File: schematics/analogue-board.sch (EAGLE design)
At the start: 81 parts, among them U1 L78S09

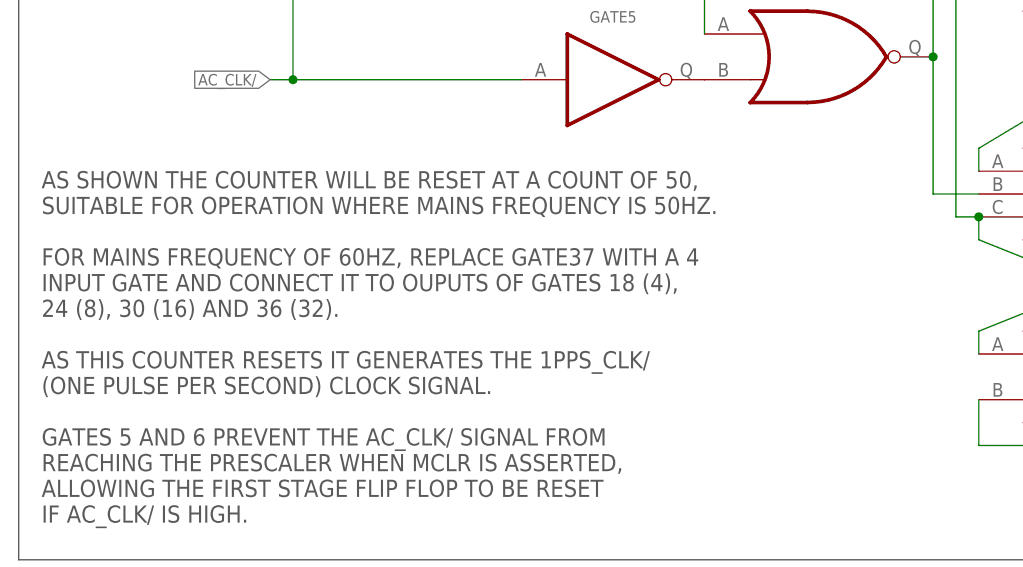
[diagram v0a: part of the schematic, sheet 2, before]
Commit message: Fixed notes for prescaler, references to incorrect gate numbers.
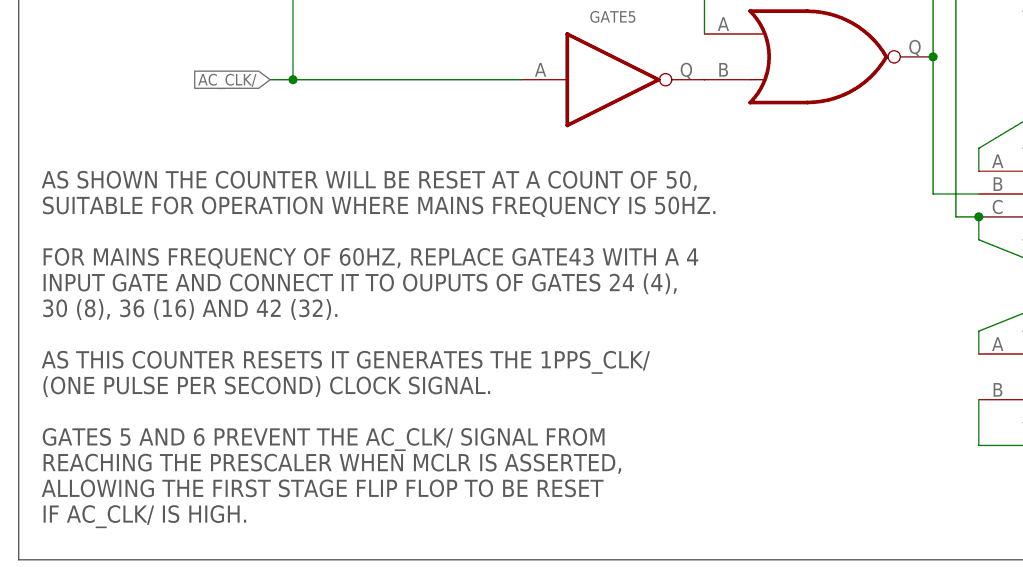
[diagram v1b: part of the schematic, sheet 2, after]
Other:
- note added: "AS SHOWN THE COUNTER WILL BE RESET AT A COUNT OF 50, SUITABLE FOR OPERATION WHERE MAINS FREQUENCY IS 50HZ. FOR MAINS FREQUENCY OF 60HZ, REPLACE GATE43 WITH A 4 INPUT GATE AND CONNECT IT TO OUPUTS OF GATES 24 (4), 30 (8), 36 (16) AND 42 (32). AS THIS COUNTER RESETS IT GENERATES THE 1PPS_CLK/ (ONE PULSE PER SECOND) CLOCK SIGNAL. GATES 5 AND 6 PREVENT THE AC_CLK/ SIGNAL FROM REACHING THE PRESCALER W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"
- note removed: "AS SHOWN THE COUNTER WILL BE RESET AT A COUNT OF 50, SUITABLE FOR OPERATION WHERE MAINS FREQUENCY IS 50HZ. FOR MAINS FREQUENCY OF 60HZ, REPLACE GATE37 WITH A 4 INPUT GATE AND CONNECT IT TO OUPUTS OF GATES 18 (4), 24 (8), 30 (16) AND 36 (32). AS THIS COUNTER RESETS IT GENERATES THE 1PPS_CLK/ (ONE PULSE PER SECOND) CLOCK SIGNAL. GATES 5 AND 6 PREVENT THE AC_CLK/ SIGNAL FROM REACHING THE PRESCALER W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"
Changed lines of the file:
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@@
 <text x="25.4" y="185.42" size="1.905" layer="97" align="top-left">AS SHOWN THE COUNTER WILL BE RESET AT A COUNT OF 50,
 SUITABLE FOR OPERATION WHERE MAINS FREQUENCY IS 50HZ.
-FOR MAINS FREQUENCY OF 60HZ, REPLACE GATE37 WITH A 4
-INPUT GATE AND CONNECT IT TO OUPUTS OF GATES 18 (4),
-24 (8), 30 (16) AND 36 (32).
+FOR MAINS FREQUENCY OF 60HZ, REPLACE GATE43 WITH A 4
+INPUT GATE AND CONNECT IT TO OUPUTS OF GATES 24 (4),
+30 (8), 36 (16) AND 42 (32).
 AS THIS COUNTER RESETS IT GENERATES THE 1PPS_CLK/
 (ONE PULSE PER SECOND) CLOCK SIGNAL.

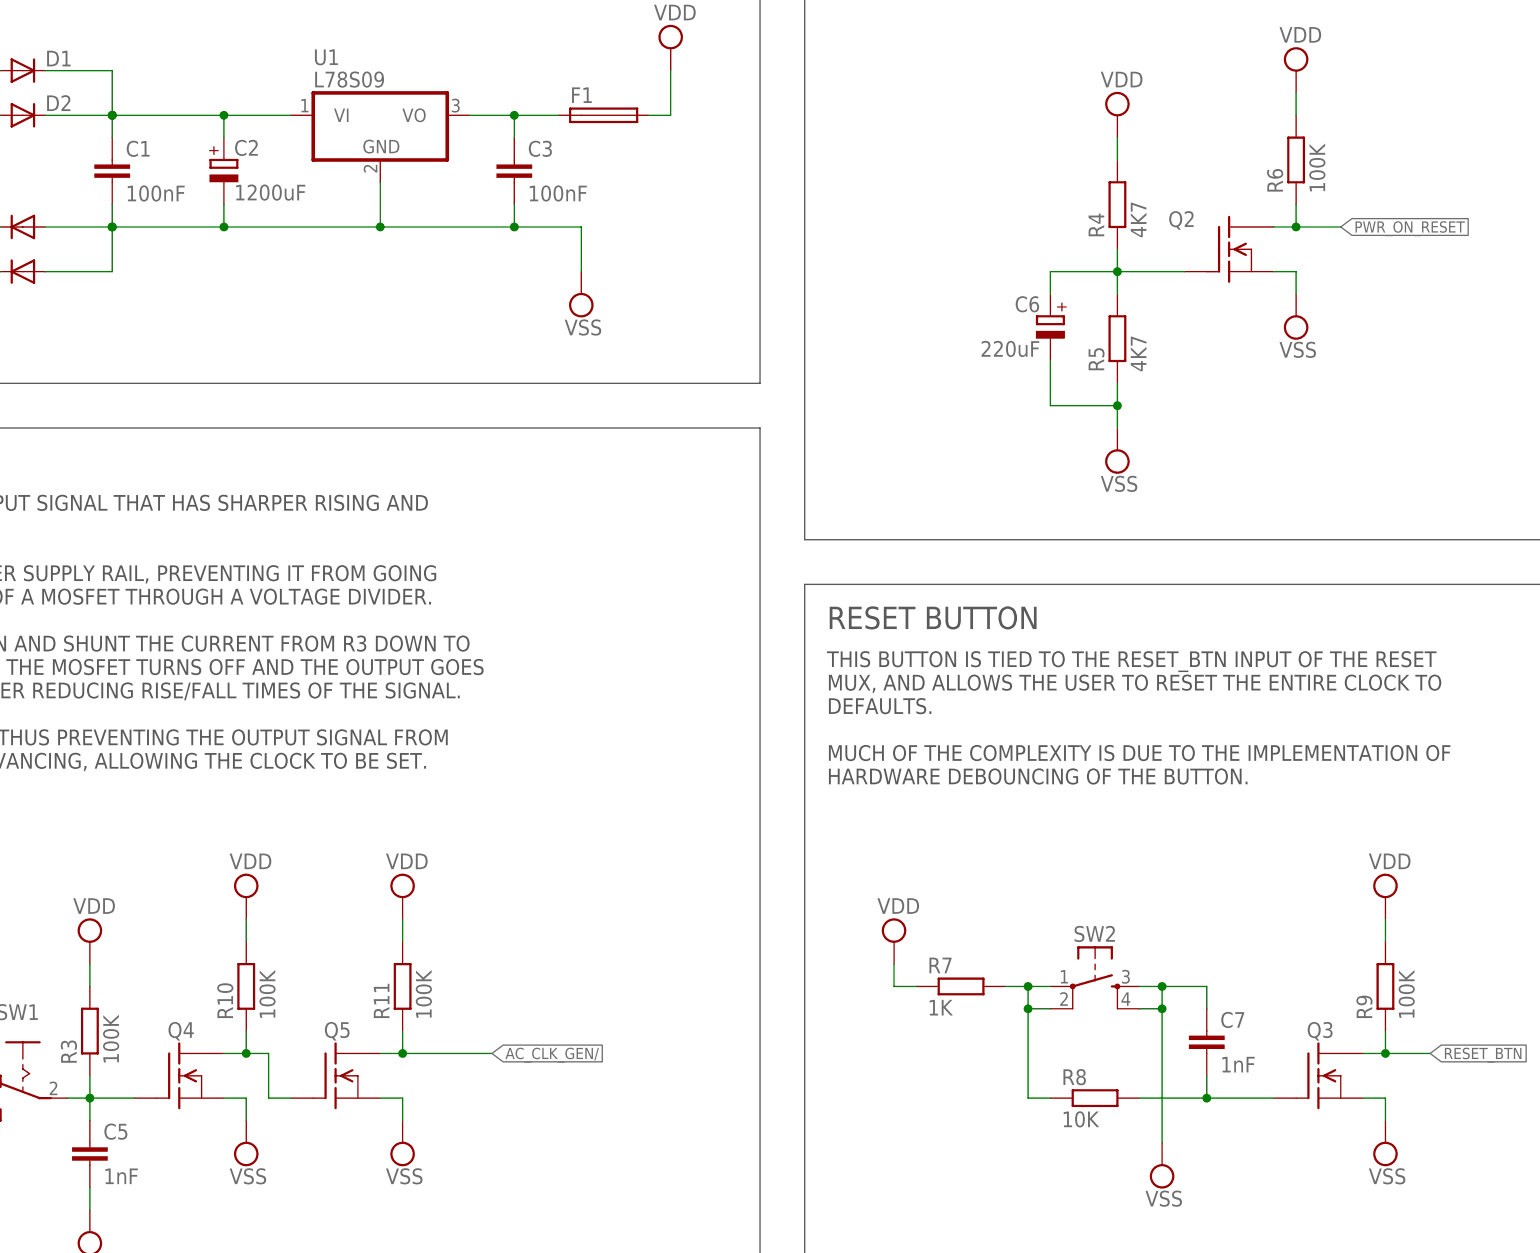
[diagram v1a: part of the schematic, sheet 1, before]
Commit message: Fix some component designators on the analogue board.
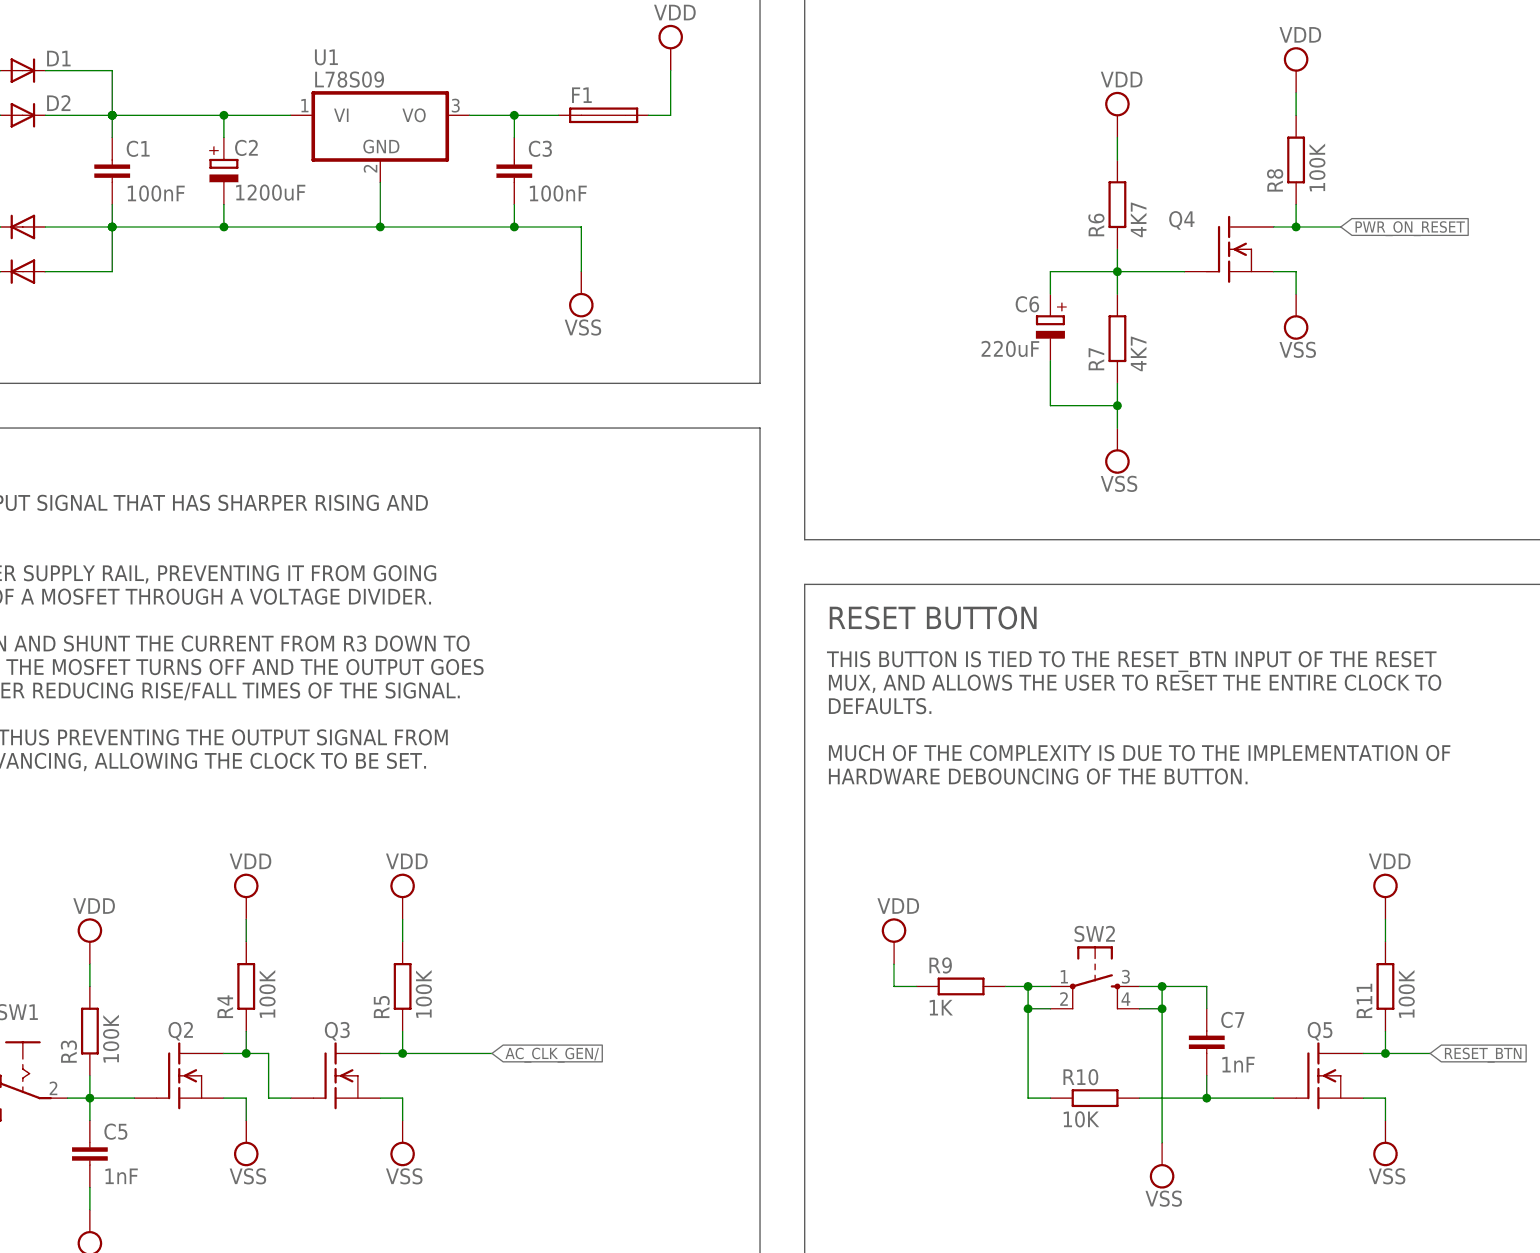
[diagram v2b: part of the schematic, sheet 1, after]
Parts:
- R10: value 100K -> 10K
- R4, R5: value 4K7 -> 100K
- R6: value 100K -> 4K7
- R7: value 1K -> 4K7
- R8: value 10K -> 100K
- R9: value 100K -> 1K
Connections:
- net AC_CLK_GEN/: now also Q3.D, R5.1; no longer Q5.D, R11.1
- net N$1: now also Q2.G; no longer Q4.G
- net N$12: now also R10.1, R9.2; no longer R7.2, R8.1
- net N$13: now also Q2.D, Q3.G, R4.1; no longer Q4.D, Q5.G, R10.1
- net N$15: now also Q5.G, R10.2; no longer Q3.G, R8.2
- net N$3: now also Q4.G, R6.1, R7.2; no longer Q2.G, R4.1, R5.2
- net PWR_ON_RESET: now also Q4.D, R8.1; no longer Q2.D, R6.1
- net RESET_BTN: now also Q5.D, R11.1; no longer Q3.D, R9.1
- net VDD: now also R5.2, R8.2, R9.1; no longer R10.2, R7.1, R9.2
- net VSS: now also R7.1; no longer R5.1
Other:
- moved on the sheet: Q2, Q3, Q4, Q5, R10, R11, R4, R5, R6, R7, R8, R9

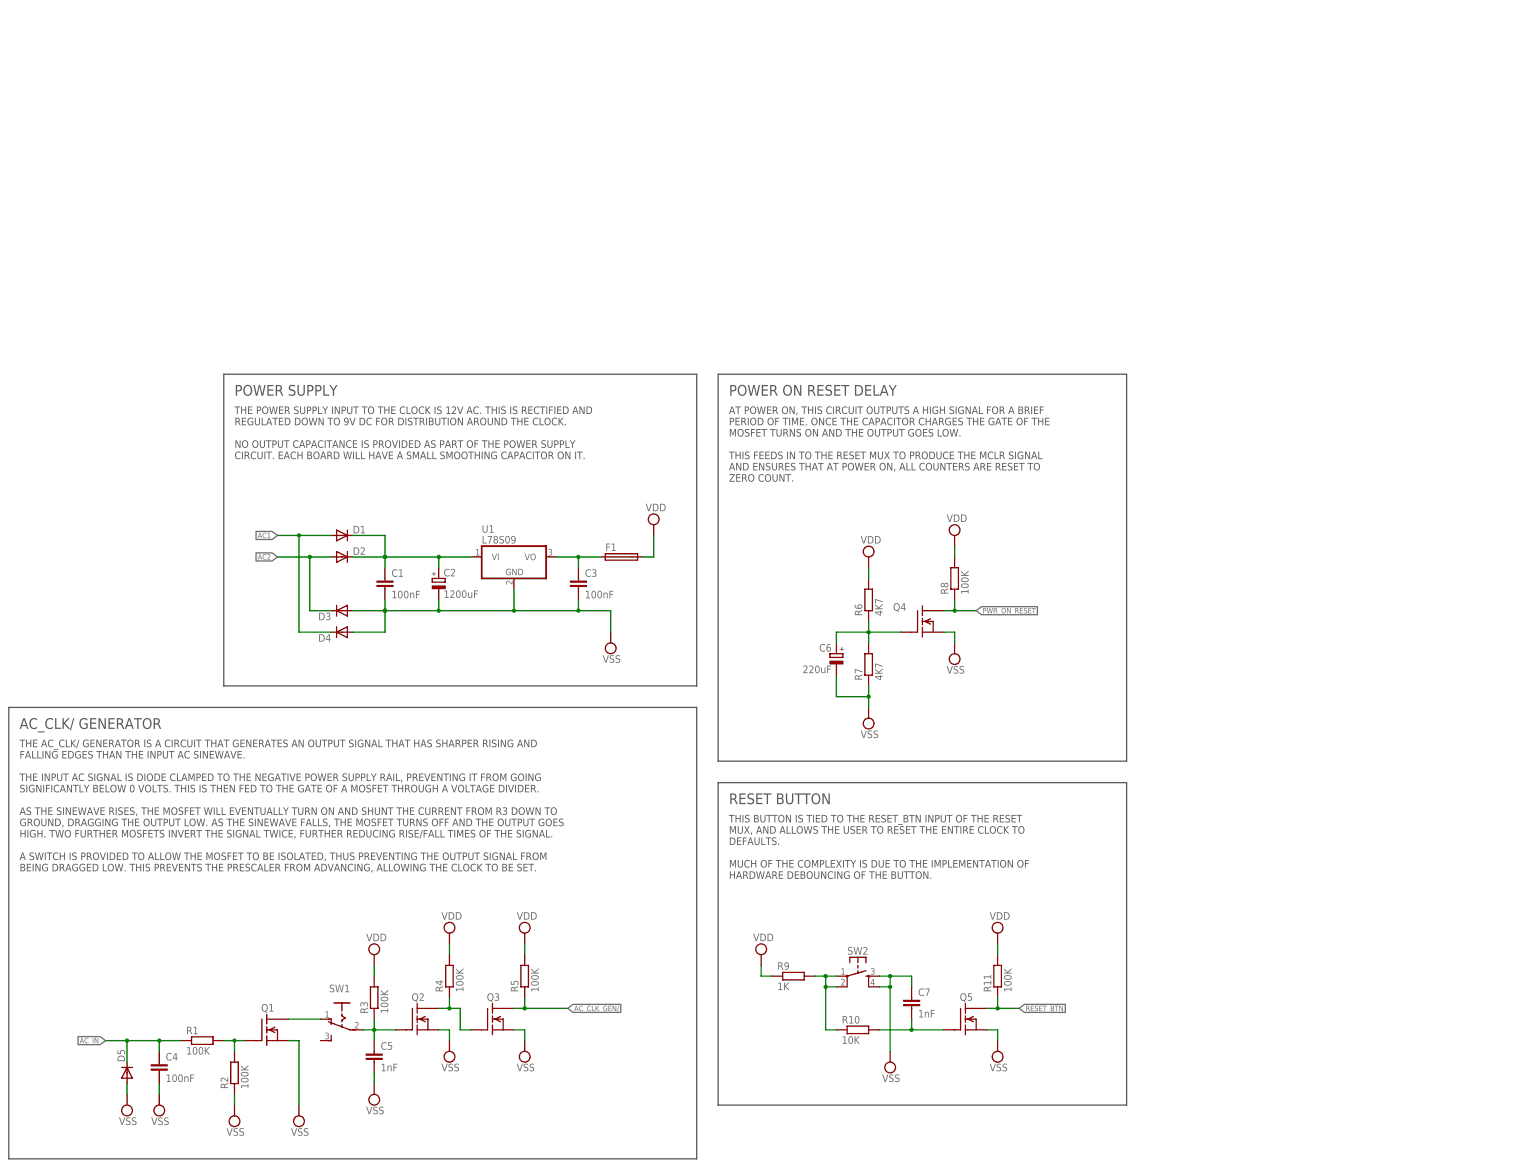
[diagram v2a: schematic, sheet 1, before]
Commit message: Modified value of C7 to 1uF from 1nF. Debounce wasnt effective enough with 1nF.
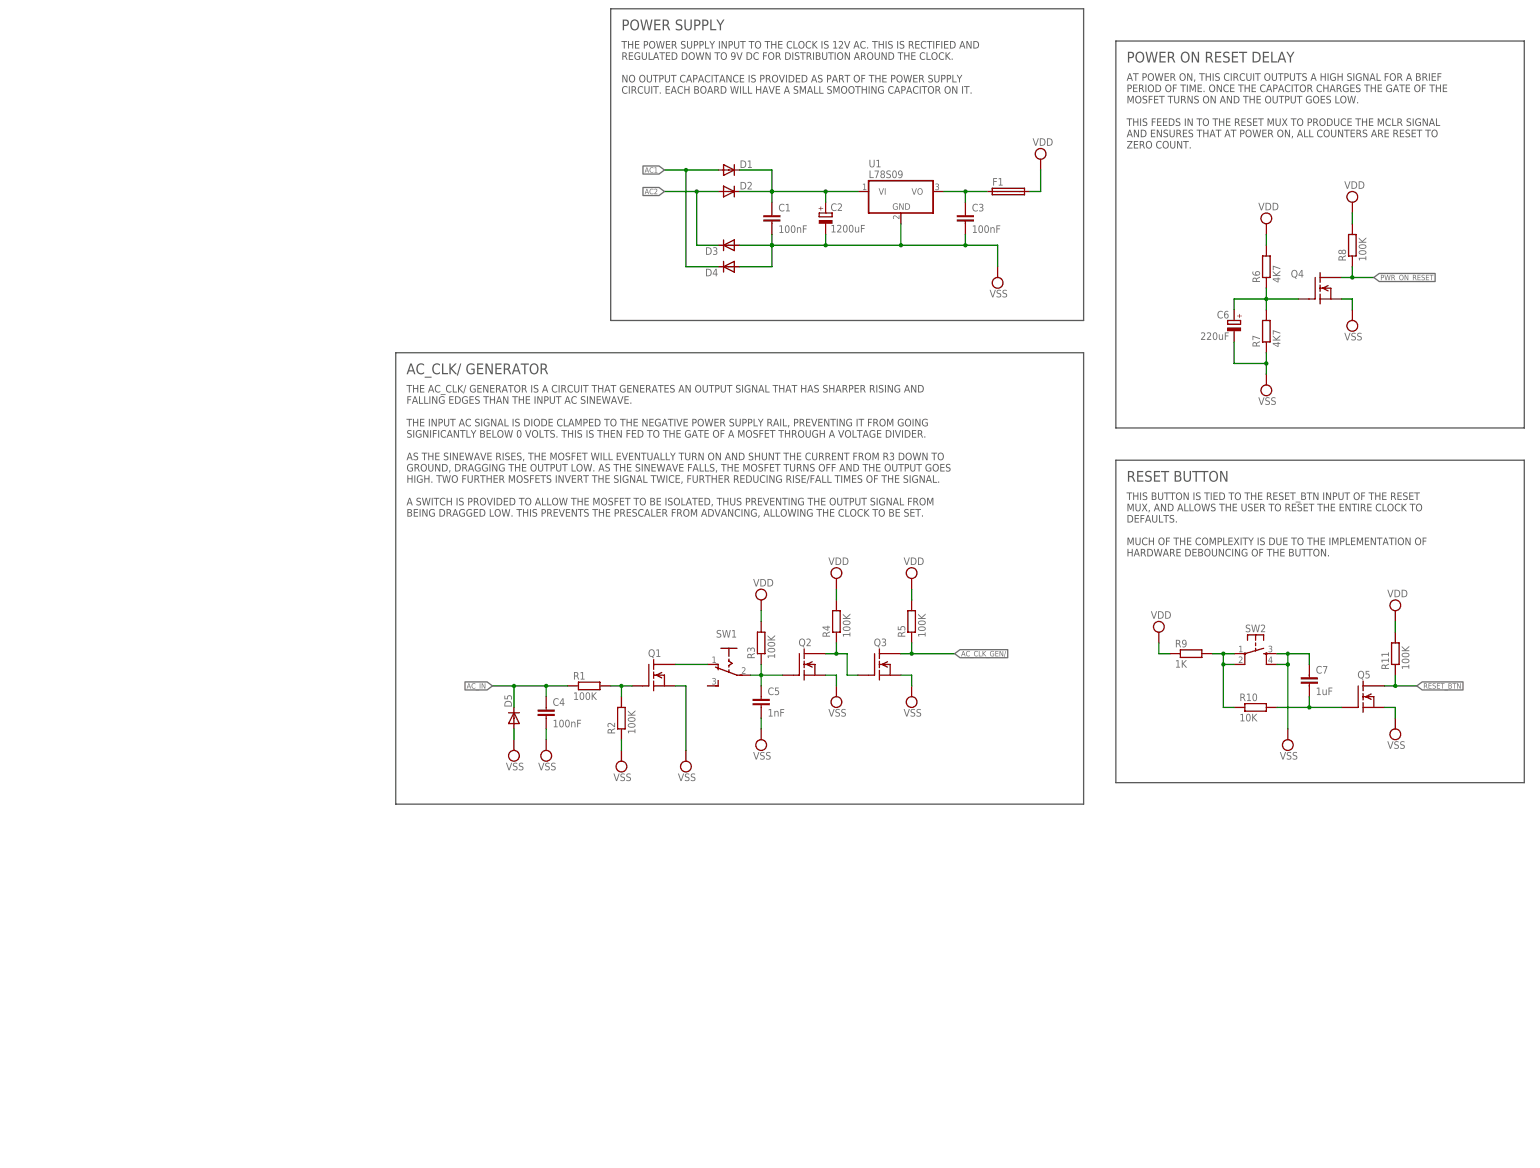
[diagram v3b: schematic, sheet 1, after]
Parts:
- C7: value 1nF -> 1uF
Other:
- moved on the sheet: C1, C2, C3, C4, C5, C6, C7, D1, D2, D3, D4, D5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
